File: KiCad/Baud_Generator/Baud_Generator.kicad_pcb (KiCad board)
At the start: 2 copper layers, 16.5 x 42.5 mm, 6 parts, among them J1 Conn_02x03_Odd_Even, J2 Conn_02x07_Odd_Even, U1 4024, X1 2.4576 MHz

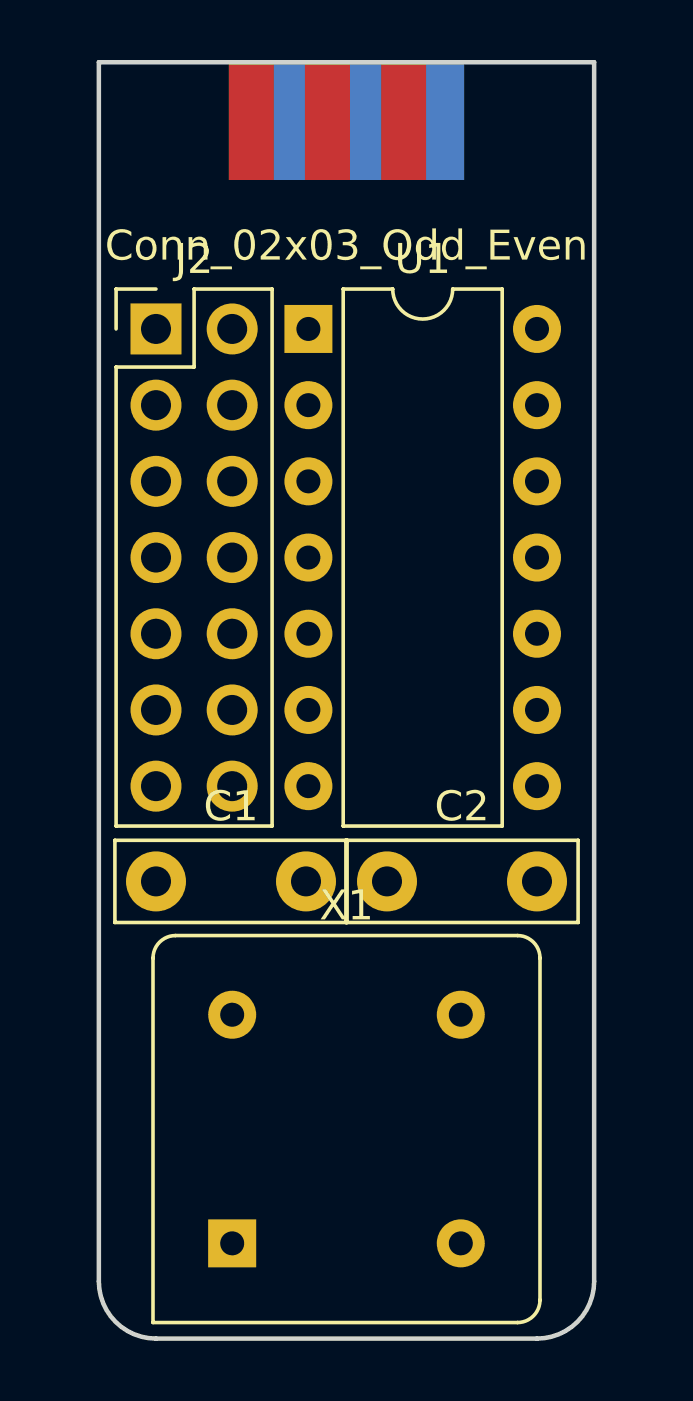
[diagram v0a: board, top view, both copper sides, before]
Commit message: Update Baud_Generator.kicad_pcb
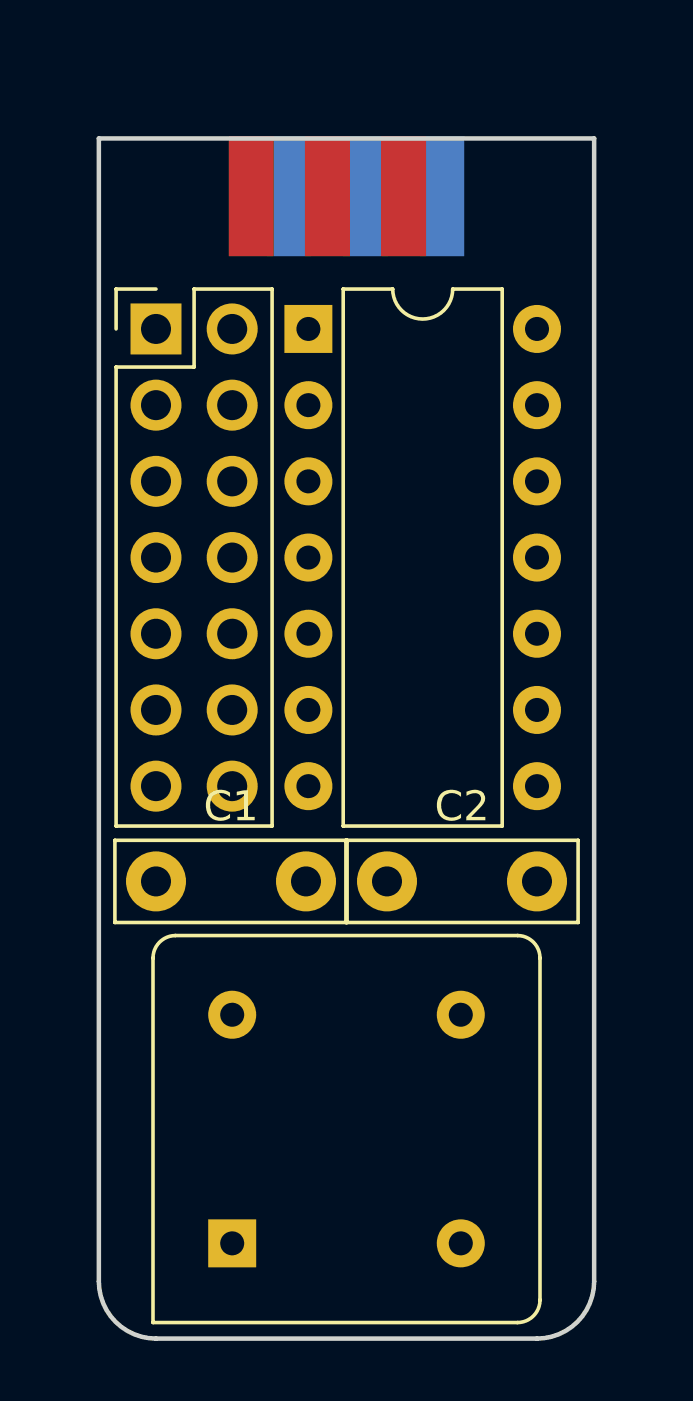
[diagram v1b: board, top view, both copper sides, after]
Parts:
- moved J1 2.54 mm to (113.6, 59.5)
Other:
- board size 16.5 x 42.5 mm -> 16.5 x 40 mm

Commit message: Completed baud rate generator PCB
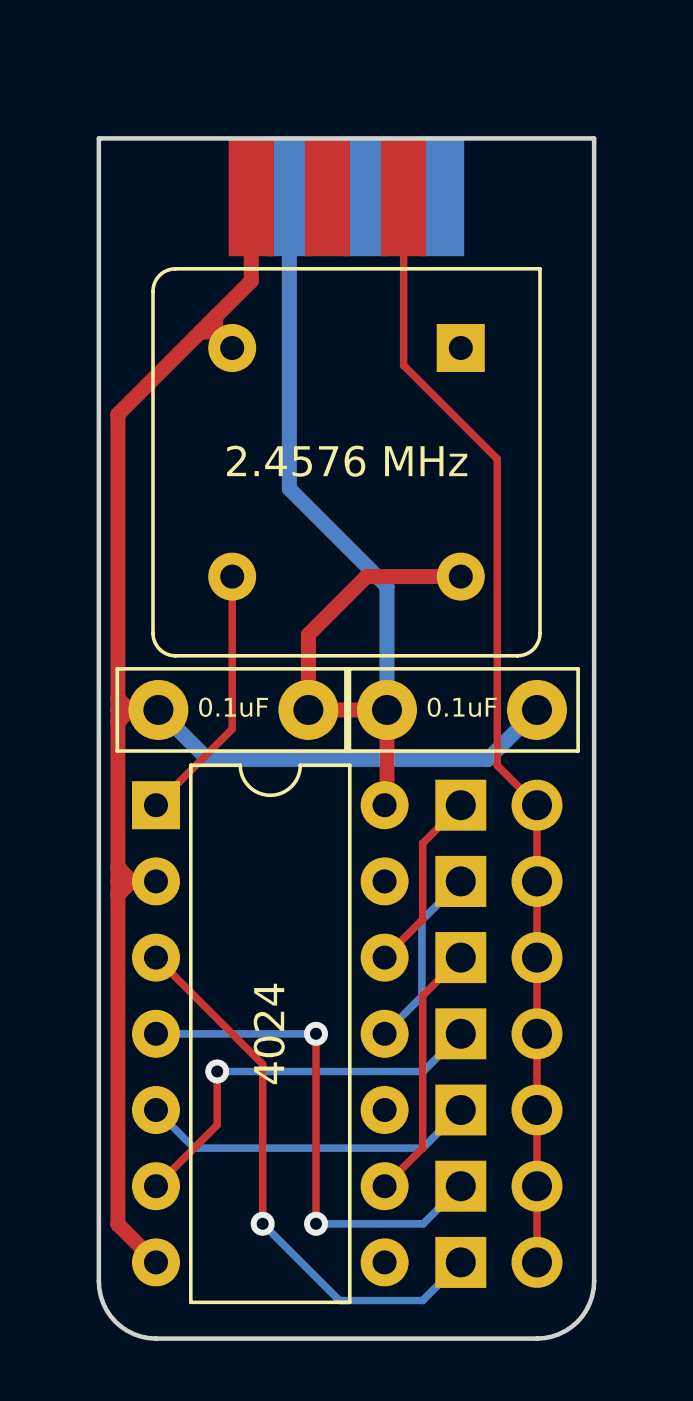
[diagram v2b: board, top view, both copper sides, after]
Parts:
- moved X1 30.8 mm to (117.4, 64.7), turned to 180 degrees
- moved J2 18.8 mm to (117.4, 79.9)
- moved U1 16.7 mm to (107.2, 79.9)
- moved 0.1uF 7.65 mm to (112.3, 76.8), turned to 180 degrees
- moved C2 5.72 mm to (114.9, 76.8)
- renumbered C1 to 0.1uF
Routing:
- net GND: track 0.00 -> 64.2 mm
- net CLOCK2: track 0.00 -> 38.0 mm
- net VCC: track 0.00 -> 32.8 mm
- net Net-(J2-Pad13): track 0.00 -> 18.4 mm, vias 0 -> 1
- net Net-(J2-Pad11): track 0.00 -> 16.8 mm, vias 0 -> 2
- net Net-(J2-Pad7): track 0.00 -> 13.3 mm, vias 0 -> 1
- net Net-(J2-Pad9): track 0.00 -> 11.2 mm
- net Net-(U1-Pad1): track 0.00 -> 8.67 mm
- net Net-(J2-Pad5): track 0.00 -> 8.67 mm
- net Net-(J2-Pad3): track 0.00 -> 6.13 mm
- net Net-(J2-Pad1): track 0.00 -> 6.13 mm

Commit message: Corrections to baud rate generator
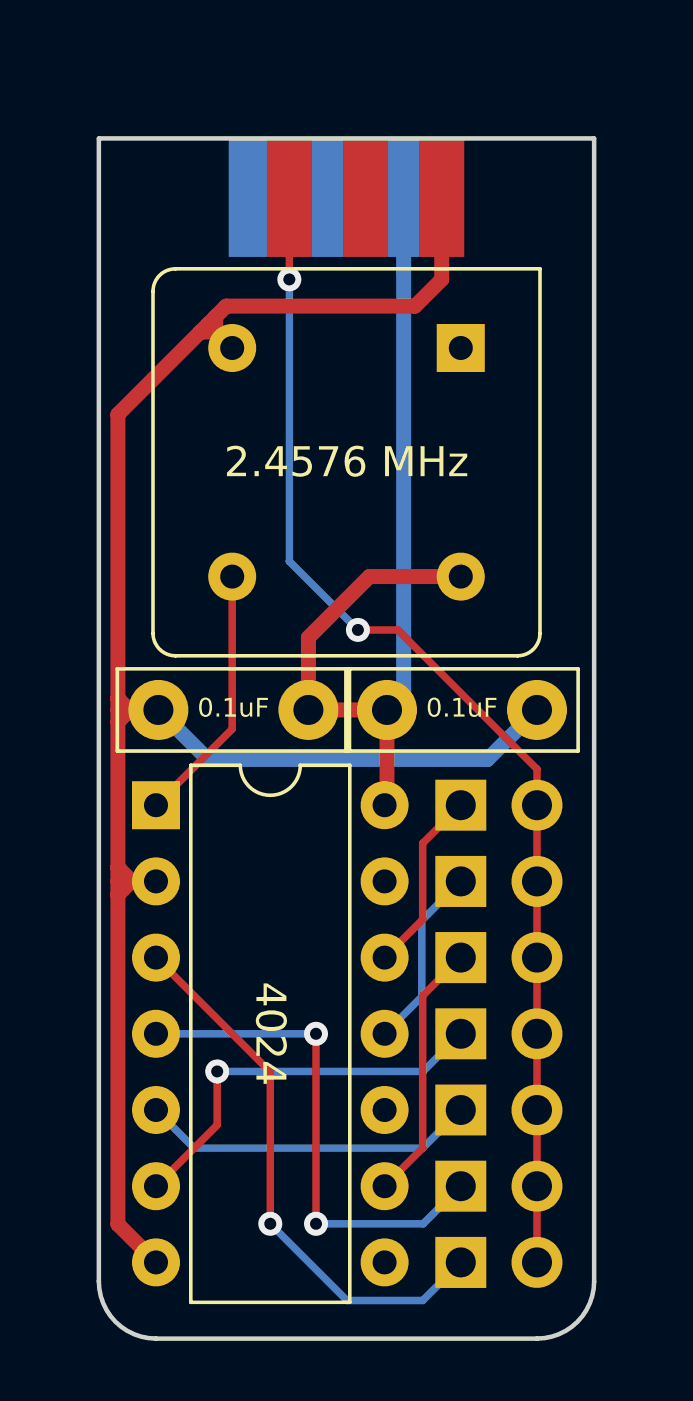
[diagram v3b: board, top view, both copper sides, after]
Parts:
- moved J1 0.28 mm to (113.6, 59.8), turned to 180 degrees
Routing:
- net GND: track 64.2 -> 70.4 mm
- net CLOCK2: track 38.0 -> 40.3 mm, vias 0 -> 2
- net VCC: track 32.8 -> 31.6 mm
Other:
- board text added: "ZF Baud Gen. @tangent3D"
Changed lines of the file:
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@@
   (general
     (thickness 1.6)
-    (drawings 8)
-    (tracks 77)
+    (drawings 9)
+    (tracks 83)
     (zones 0)
     (modules 6)
@@
     (pad_to_mask_clearance 0)
     (aux_axis_origin 0 0)
-    (grid_origin 107.235001 76.755001)
+    (grid_origin 105.330001 57.705001)
     (visible_elements 7FFFFFFF)
     (pcbplotparams
@@
     (fp_line (start 6.5 -1.5) (end -1.5 -1.5) (layer F.CrtYd) (width 0.05))
     (fp_text user 0.1uF (at 2.5 -0.0675) (layer F.SilkS)
-      (effects (font (size 0.625 0.625) (thickness 0.15)))
+      (effects (font (size 0.625 0.625) (thickness 0.125)))
     )
     (pad 1 thru_hole circle (at 0 0) (size 2 2) (drill 1) (layers *.Cu *.Mask)
@@
   )
   (module Baud_Generator:ZF_CPU_Control_Header (layer F.Cu)
-    (at 113.585001 59.503)
+    (at 113.585001 59.782 180)
     (fp_text reference J1 (at 0 -5.08 180) (layer F.SilkS) hide
       (effects (font (size 1 1) (thickness 0.15)))
@@
       (effects (font (size 1 1) (thickness 0.15)))
     )
-    (pad 6 connect rect (at 3.175 0.127 180) (size 1.5 4) (layers B.Cu)
+    (pad 1 connect rect (at -3.175 0.127) (size 1.5 4) (layers F.Cu)
+      (net 1 GND))
+    (pad 3 connect rect (at -0.635 0.127) (size 1.5 4) (layers F.Cu)
+      (net 6 "Net-(J1-Pad3)"))
+    (pad 5 connect rect (at 1.905 0.127) (size 1.5 4) (layers F.Cu)
+      (net 5 CLOCK2))
+    (pad 2 connect rect (at -1.905 0.127) (size 1.5 4) (layers B.Cu)
+      (net 2 VCC))
+    (pad 4 connect rect (at 0.635 0.127) (size 1.5 4) (layers B.Cu)
+      (net 4 "Net-(J1-Pad4)"))
+    (pad 6 connect rect (at 3.175 0.127) (size 1.5 4) (layers B.Cu)
       (net 3 "Net-(J1-Pad6)"))
-    (pad 4 connect rect (at 0.635 0.127 180) (size 1.5 4) (layers B.Cu)
-      (net 4 "Net-(J1-Pad4)"))
-    (pad 2 connect rect (at -1.905 0.127 180) (size 1.5 4) (layers B.Cu)
-      (net 2 VCC))
-    (pad 5 connect rect (at 1.905 0.127 180) (size 1.5 4) (layers F.Cu)
-      (net 5 CLOCK2))
-    (pad 3 connect rect (at -0.635 0.127 180) (size 1.5 4) (layers F.Cu)
-      (net 6 "Net-(J1-Pad3)"))
-    (pad 1 connect rect (at -3.175 0.127 180) (size 1.5 4) (layers F.Cu)
-      (net 1 GND))
   )
   (module Package_DIP:DIP-14_W7.62mm (layer F.Cu)
@@
     (fp_line (start 6.985 -1.27) (end 6.985 16.51) (layer F.Fab) (width 0.1))
     (fp_line (start 1.635 -1.27) (end 6.985 -1.27) (layer F.Fab) (width 0.1))
-    (fp_text user 4024 (at 3.81 7.62 90) (layer F.SilkS)
+    (fp_text user 4024 (at 3.81 7.62 270 unlocked) (layer F.SilkS)
       (effects (font (size 1 1) (thickness 0.15)))
     )
@@
       (rotate (xyz 0 0 0))
     )
+  )
+  (gr_text "ZF Baud Gen.\n@tangent3D" (at 113.585001 68.500001) (layer B.SilkS)
+    (effects (font (size 1.5 1.5) (thickness 0.25)) (justify mirror))
   )
   (gr_arc (start 107.235001 95.805001) (end 105.330001 95.805001) (angle -90) (layer Edge.Cuts) (width 0.15))
@@
   (segment (start 107.235001 82.470001) (end 106.410001 82.470001) (width 0.5) (layer F.Cu) (net 1))
   (segment (start 105.965001 82.005001) (end 105.965001 82.915001) (width 0.5) (layer F.Cu) (net 1))
-  (segment (start 110.375001 59.665) (end 110.410001 59.63) (width 0.5) (layer F.Cu) (net 1))
-  (segment (start 110.410001 62.460001) (end 110.410001 59.63) (width 0.5) (layer F.Cu) (net 1))
   (segment (start 105.965001 76.375001) (end 105.965001 66.905001) (width 0.5) (layer F.Cu) (net 1))
   (segment (start 105.965001 66.905001) (end 108.715001 64.155001) (width 0.5) (layer F.Cu) (net 1))
   (segment (start 108.715001 64.155001) (end 108.980001 63.890001) (width 0.5) (layer F.Cu) (net 1))
   (segment (start 108.980001 63.890001) (end 109.225001 63.645001) (width 0.5) (layer F.Cu) (net 1))
-  (segment (start 109.225001 63.645001) (end 110.410001 62.460001) (width 0.5) (layer F.Cu) (net 1))
   (segment (start 109.775001 64.685001) (end 108.980001 63.890001) (width 0.5) (layer F.Cu) (net 1))
   (segment (start 109.225001 64.140001) (end 109.775001 64.690001) (width 0.5) (layer F.Cu) (net 1))
@@
   (segment (start 108.965001 78.405001) (end 118.285001 78.405001) (width 0.5) (layer B.Cu) (net 1))
   (segment (start 107.315001 76.755001) (end 108.965001 78.405001) (width 0.5) (layer B.Cu) (net 1))
-  (segment (start 114.250001 72.310001) (end 117.395001 72.310001) (width 0.5) (layer F.Cu) (net 2))
-  (segment (start 112.315001 74.245001) (end 114.250001 72.310001) (width 0.5) (layer F.Cu) (net 2))
-  (segment (start 112.315001 76.755001) (end 112.315001 74.245001) (width 0.5) (layer F.Cu) (net 2))
+  (segment (start 116.760001 59.655) (end 116.760001 62.404001) (width 0.5) (layer F.Cu) (net 1))
+  (segment (start 109.577001 63.293001) (end 109.225001 63.645001) (width 0.5) (layer F.Cu) (net 1))
+  (segment (start 116.760001 62.404001) (end 115.871001 63.293001) (width 0.5) (layer F.Cu) (net 1))
+  (segment (start 115.871001 63.293001) (end 109.577001 63.293001) (width 0.5) (layer F.Cu) (net 1))
   (segment (start 114.855001 76.675001) (end 114.935001 76.755001) (width 0.5) (layer F.Cu) (net 2))
   (segment (start 114.935001 79.850001) (end 114.855001 79.930001) (width 0.5) (layer F.Cu) (net 2))
   (segment (start 114.935001 76.755001) (end 114.935001 79.850001) (width 0.5) (layer F.Cu) (net 2))
-  (segment (start 114.935001 72.635001) (end 111.680001 69.380001) (width 0.5) (layer B.Cu) (net 2))
-  (segment (start 114.935001 76.755001) (end 114.935001 72.635001) (width 0.5) (layer B.Cu) (net 2))
-  (segment (start 111.680001 69.380001) (end 111.680001 59.63) (width 0.5) (layer B.Cu) (net 2))
   (segment (start 112.315001 76.755001) (end 114.935001 76.755001) (width 0.5) (layer F.Cu) (net 2))
+  (segment (start 112.315001 74.342001) (end 114.347001 72.310001) (width 0.5) (layer F.Cu) (net 2))
+  (segment (start 114.347001 72.310001) (end 117.395001 72.310001) (width 0.5) (layer F.Cu) (net 2))
+  (segment (start 112.315001 76.755001) (end 112.315001 74.342001) (width 0.5) (layer F.Cu) (net 2))
+  (segment (start 114.982001 76.708001) (end 114.935001 76.755001) (width 0.25) (layer B.Cu) (net 2))
+  (segment (start 115.490001 62.150001) (end 115.490001 59.655) (width 0.5) (layer B.Cu) (net 2))
+  (segment (start 115.490001 76.200001) (end 115.490001 62.150001) (width 0.5) (layer B.Cu) (net 2))
+  (segment (start 114.982001 76.708001) (end 115.490001 76.200001) (width 0.5) (layer B.Cu) (net 2))
   (segment (start 119.935001 79.930001) (end 119.935001 95.170001) (width 0.25) (layer F.Cu) (net 5))
   (segment (start 119.935001 79.325001) (end 119.935001 79.930001) (width 0.25) (layer F.Cu) (net 5))
-  (segment (start 115.490001 65.270001) (end 115.490001 59.63) (width 0.25) (layer F.Cu) (net 5))
-  (segment (start 118.61 68.39) (end 115.490001 65.270001) (width 0.25) (layer F.Cu) (net 5))
-  (segment (start 118.61 78.605) (end 118.61 68.39) (width 0.25) (layer F.Cu) (net 5))
-  (segment (start 119.935001 79.930001) (end 118.61 78.605) (width 0.25) (layer F.Cu) (net 5))
+  (via (at 113.966001 74.088001) (size 0.8) (drill 0.4) (layers F.Cu B.Cu) (net 5))
+  (via (at 111.680001 62.404001) (size 0.8) (drill 0.4) (layers F.Cu B.Cu) (net 5))
+  (segment (start 111.680001 59.655) (end 111.680001 62.404001) (width 0.25) (layer F.Cu) (net 5))
+  (segment (start 119.935001 79.930001) (end 119.935001 78.72792) (width 0.25) (layer F.Cu) (net 5))
+  (segment (start 119.935001 78.72792) (end 115.295082 74.088001) (width 0.25) (layer F.Cu) (net 5))
+  (segment (start 115.295082 74.088001) (end 113.966001 74.088001) (width 0.25) (layer F.Cu) (net 5))
+  (segment (start 111.680001 71.802001) (end 111.680001 62.404001) (width 0.25) (layer B.Cu) (net 5))
+  (segment (start 113.966001 74.088001) (end 111.680001 71.802001) (width 0.25) (layer B.Cu) (net 5))
   (segment (start 109.775001 77.390001) (end 107.235001 79.930001) (width 0.25) (layer F.Cu) (net 7))
   (segment (start 109.775001 72.310001) (end 109.775001 77.390001) (width 0.25) (layer F.Cu) (net 7))
@@
   (segment (start 116.142001 93.883001) (end 112.679001 93.883001) (width 0.25) (layer B.Cu) (net 14))
   (segment (start 117.395001 92.630001) (end 116.142001 93.883001) (width 0.25) (layer B.Cu) (net 14))
-  (segment (start 110.791001 88.566001) (end 110.791001 93.773001) (width 0.25) (layer F.Cu) (net 15))
-  (segment (start 107.235001 85.010001) (end 110.791001 88.566001) (width 0.25) (layer F.Cu) (net 15))
-  (via (at 110.791001 93.883001) (size 0.8) (drill 0.4) (layers F.Cu B.Cu) (net 15))
-  (segment (start 113.348001 96.440001) (end 110.791001 93.883001) (width 0.25) (layer B.Cu) (net 15))
-  (segment (start 116.125001 96.440001) (end 113.348001 96.440001) (width 0.25) (layer B.Cu) (net 15))
+  (via (at 111.045001 93.883001) (size 0.8) (drill 0.4) (layers F.Cu B.Cu) (net 15))
+  (segment (start 111.045001 88.820001) (end 111.045001 93.519001) (width 0.25) (layer F.Cu) (net 15))
+  (segment (start 107.235001 85.010001) (end 111.045001 88.820001) (width 0.25) (layer F.Cu) (net 15))
+  (segment (start 113.602001 96.440001) (end 111.045001 93.883001) (width 0.25) (layer B.Cu) (net 15))
+  (segment (start 116.125001 96.440001) (end 113.602001 96.440001) (width 0.25) (layer B.Cu) (net 15))
   (segment (start 117.395001 95.170001) (end 116.125001 96.440001) (width 0.25) (layer B.Cu) (net 15))
 )

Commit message: Changed edge connector, Gerber settings
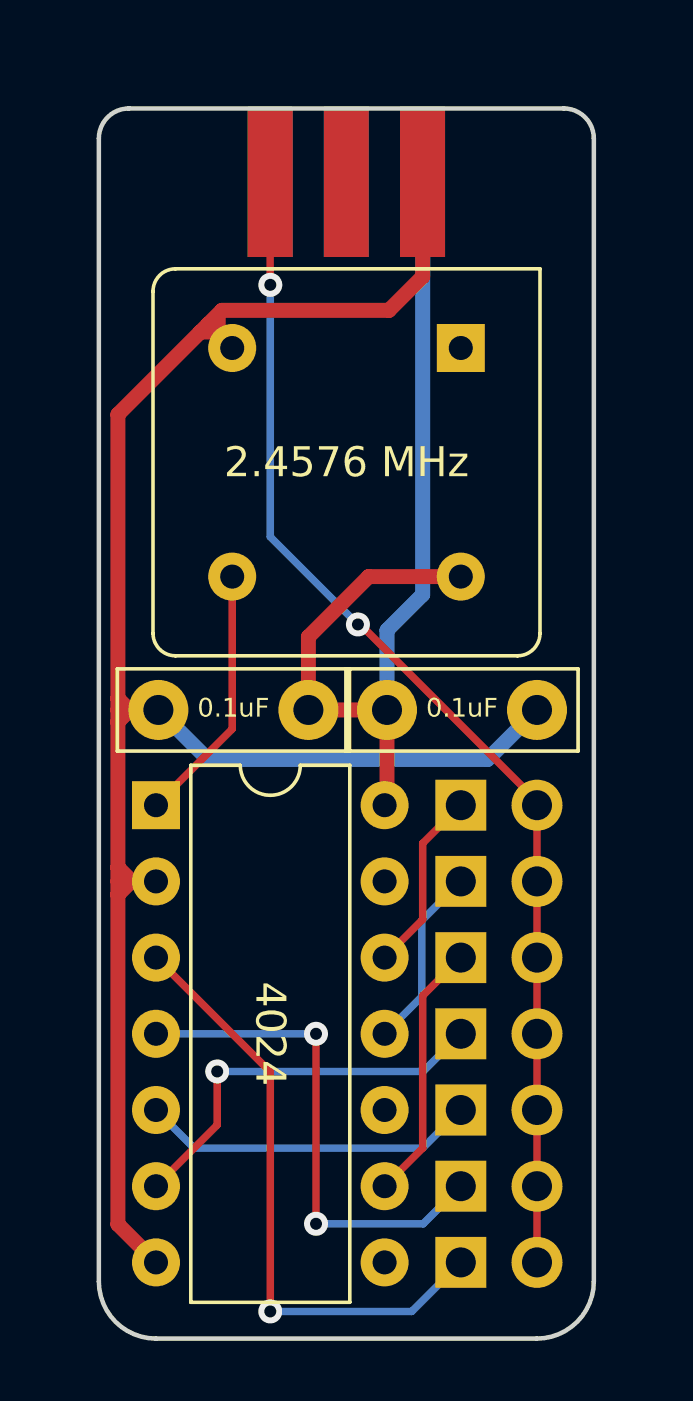
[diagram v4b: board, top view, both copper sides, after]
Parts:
- moved J1 0.63 mm to (113.6, 59.2)
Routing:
- net Net-(J2-Pad13): track 18.0 -> 20.4 mm
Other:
- board size 16.5 x 40 mm -> 16.5 x 41 mm
